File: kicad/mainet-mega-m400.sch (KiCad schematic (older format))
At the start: 4 parts, among them J40 Screw_Terminal_01x04, J64 Screw_Terminal_01x09, J65 Screw_Terminal_01x17, J66 Screw_Terminal_01x02

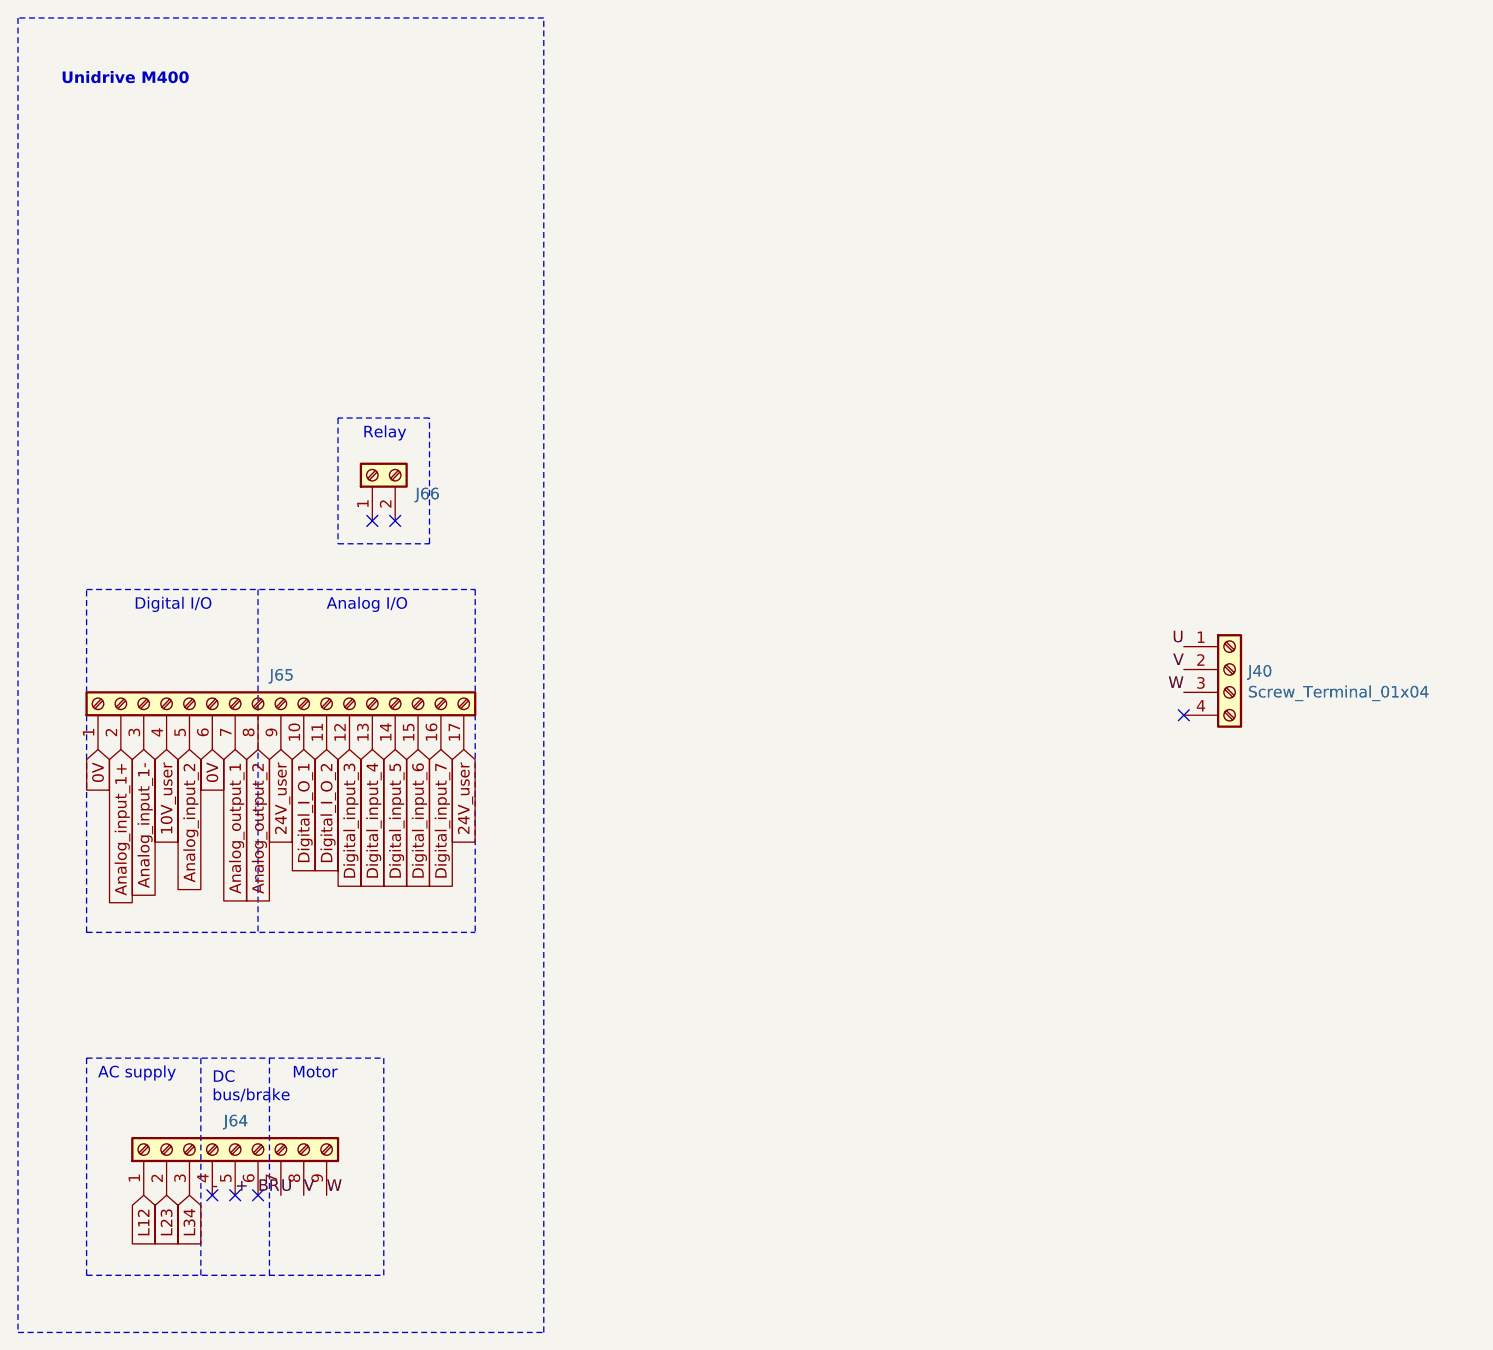
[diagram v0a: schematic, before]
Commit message: Kicad: Modificaciones menores esquemáticos
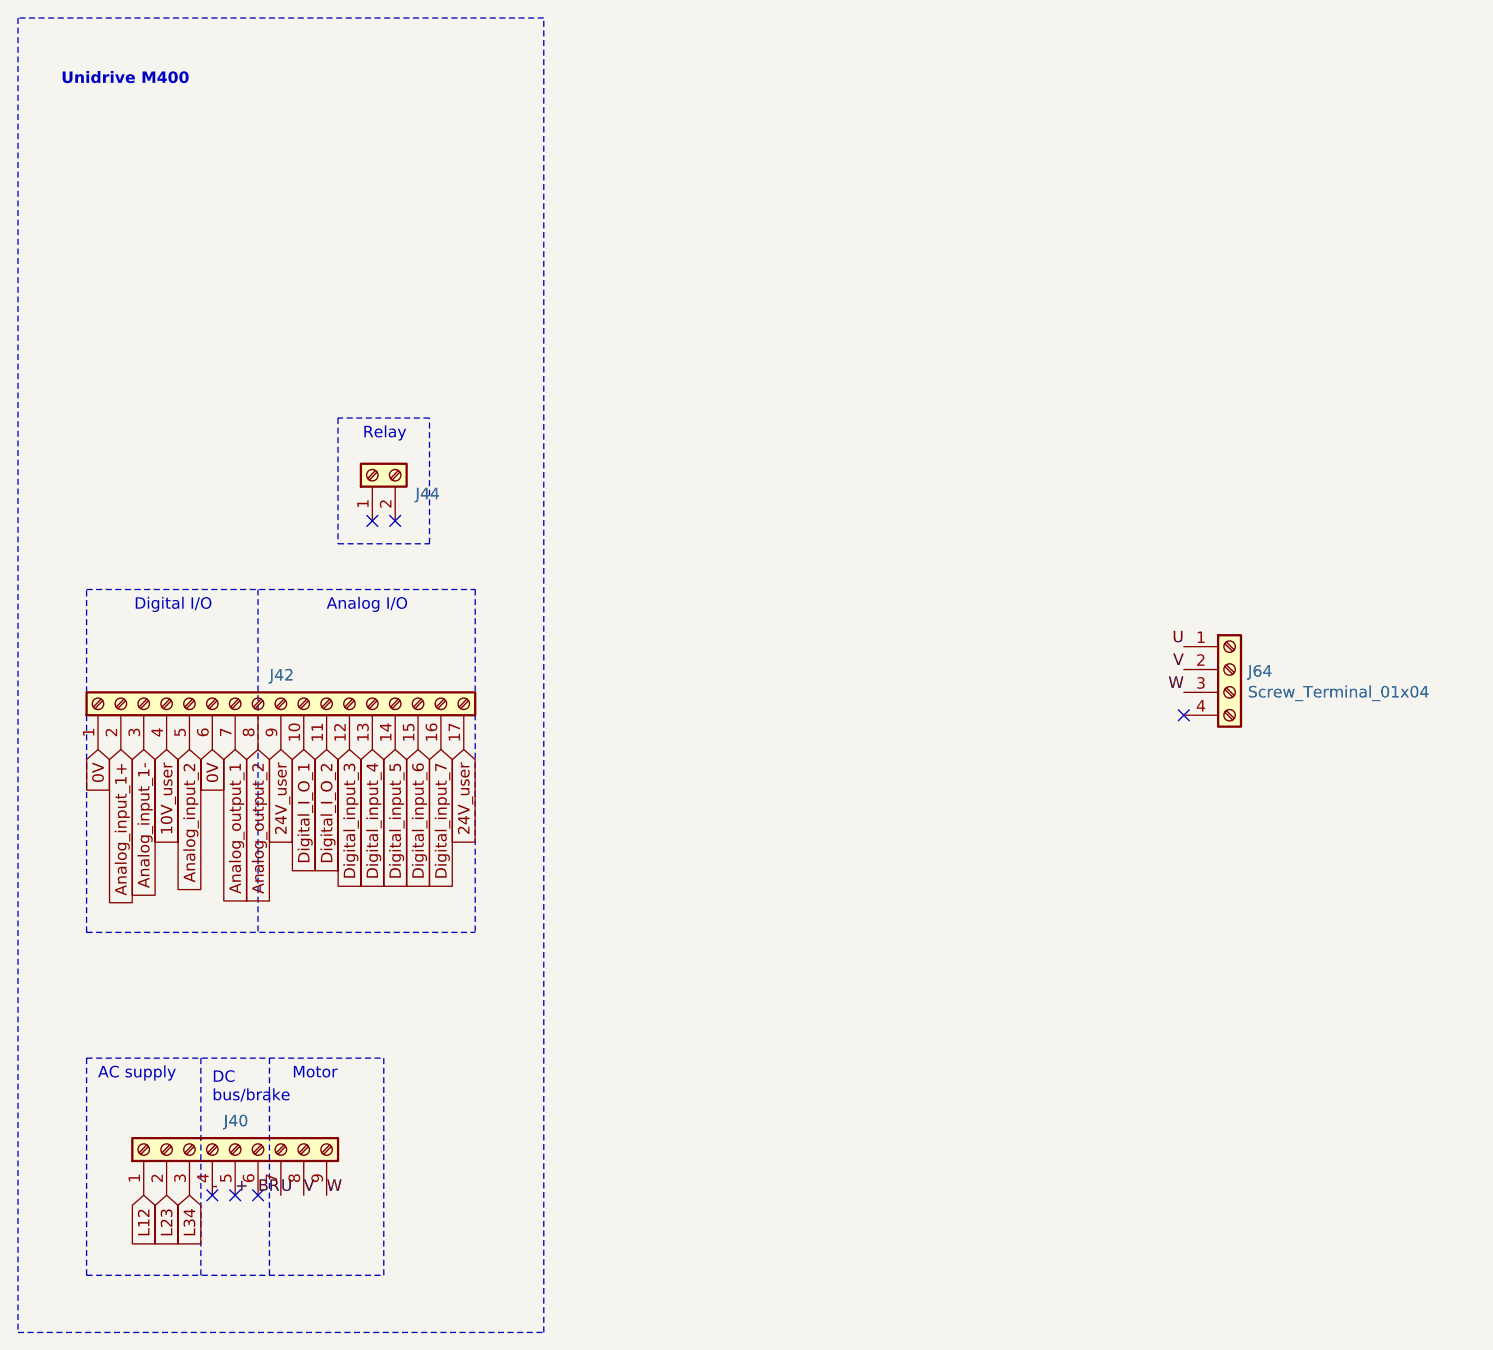
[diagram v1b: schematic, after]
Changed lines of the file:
@@
 $Descr A4 11693 8268
 encoding utf-8
-Sheet 14 17
+Sheet 17 17
 Title ""
 Date ""
@@
 U 1 1 5FF5E302
 P 3500 4400
-F 0 "J65" V 3625 4396 50  0000 C CNN
+AR Path="/5FC25793/5FF5E17E/5FF5E302" Ref="J65"  Part="1"
+AR Path="/601B5E4D/5FF5E302" Ref="J42"  Part="1"
+F 0 "J42" V 3625 4396 50  0000 C CNN
 F 1 "Screw_Terminal_01x17" H 3580 4351 50  0001 L CNN
 F 2 "" H 3500 4400 50  0001 C CNN
@@
 U 1 1 5FF6D0E6
 P 3900 3400
-F 0 "J66" V 3818 3212 50  0000 R CNN
+AR Path="/5FC25793/5FF5E17E/5FF6D0E6" Ref="J66"  Part="1"
+AR Path="/601B5E4D/5FF6D0E6" Ref="J44"  Part="1"
+F 0 "J44" V 3818 3212 50  0000 R CNN
 F 1 "Screw_Terminal_01x02" V 3773 3212 50  0001 R CNN
 F 2 "" H 3900 3400 50  0001 C CNN
@@
 U 1 1 5FF6E669
 P 3300 6350
-F 0 "J64" V 3425 6346 50  0000 C CNN
+AR Path="/5FC25793/5FF5E17E/5FF6E669" Ref="J64"  Part="1"
+AR Path="/601B5E4D/5FF6E669" Ref="J40"  Part="1"
+F 0 "J40" V 3425 6346 50  0000 C CNN
 F 1 "Screw_Terminal_01x09" V 3426 6346 50  0001 C CNN
 F 2 "" H 3300 6350 50  0001 C CNN
@@
 U 1 1 5FE3097B
 P 7650 4250
-F 0 "J40" H 7730 4242 50  0000 L CNN
+AR Path="/5FC25793/5FF5E17E/5FE3097B" Ref="J40"  Part="1"
+AR Path="/601B5E4D/5FE3097B" Ref="J64"  Part="1"
+F 0 "J64" H 7730 4242 50  0000 L CNN
 F 1 "Screw_Terminal_01x04" H 7730 4151 50  0000 L CNN
 F 2 "" H 7650 4250 50  0001 C CNN
